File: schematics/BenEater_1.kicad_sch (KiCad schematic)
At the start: 12 parts, among them SW1 RESET, U1 W65C02SxP, U2 28C256, U3 W65C22SxP, U4 74HC00, U6 HM62256BLP, X1 ACO-1 MHz

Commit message: correct schematic
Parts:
- DS1: value WC1602A -> 16x2 LCD
- U6: value HM62256BLP -> 62256
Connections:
- net VCC is gone; now on net +5V: U4.1, U4.2, U4.5
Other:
- note added: "A"
- note added: "K"
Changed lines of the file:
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@@
 		)
 	)
+	(text "A"
+		(exclude_from_sim no)
+		(at 239.522 132.08 0)
+		(effects
+			(font
+				(size 1.27 1.27)
+			)
+		)
+	)
 	(text ""
 		(exclude_from_sim no)
@@
 		)
 	)
+	(text "K"
+		(exclude_from_sim no)
+		(at 239.522 134.874 0)
+		(effects
+			(font
+				(size 1.27 1.27)
+			)
+		)
+	)
 	(label "Reset"
 		(at 26.67 72.39 0)
@@
 		)
 	)
-	(hierarchical_label "VCC"
-		(shape input)
-		(at 40.64 30.48 180)
-		(effects
-			(font
-				(size 1.27 1.27)
-			)
-			(justify right)
-		)
-	)
-	(hierarchical_label "VCC"
-		(shape input)
-		(at 40.64 50.8 180)
-		(effects
-			(font
-				(size 1.27 1.27)
-			)
-			(justify right)
-		)
-	)
-	(hierarchical_label "VCC"
-		(shape input)
-		(at 40.64 35.56 180)
-		(effects
-			(font
-				(size 1.27 1.27)
-			)
-			(justify right)
-		)
-	)
 	(symbol
 		(lib_id "power:GND")
@@
 			)
 		)
-		(property "Value" "WC1602A"
+		(property "Value" "16x2 LCD"
 			(at 242.2241 119.38 0)
 			(effects
@@
 			)
 		)
-		(property "Value" "HM62256BLP"
+		(property "Value" "62256"
 			(at 92.3641 121.92 0)
 			(effects
@@
 	)
 	(symbol
+		(lib_id "power:+5V")
+		(at 40.64 50.8 90)
+		(unit 1)
+		(exclude_from_sim no)
+		(in_bom yes)
+		(on_board yes)
+		(dnp no)
+		(fields_autoplaced yes)
+		(property "Reference" "#PWR021"
+			(at 44.45 50.8 0)
+			(effects
+				(font
+					(size 1.27 1.27)
+				)
+				(hide yes)
+			)
+		)
+		(property "Value" "+5V"
+			(at 36.83 50.7999 90)
+			(effects
+				(font
+					(size 1.27 1.27)
+				)
+				(justify left)
+			)
+		)
+		(property "Footprint" ""
+			(at 40.64 50.8 0)
+			(effects
+				(font
+					(size 1.27 1.27)
+				)
+				(hide yes)
+			)
+		)
+		(property "Datasheet" ""
+			(at 40.64 50.8 0)
+			(effects
+				(font
+					(size 1.27 1.27)
+				)
+				(hide yes)
+			)
+		)
+		(property "Description" "Power symbol creates a global label with name \"+5V\""
+			(at 40.64 50.8 0)
+			(effects
+				(font
+					(size 1.27 1.27)
+				)
+				(hide yes)
+			)
+		)
+		(pin "1"
+		)
+		(instances
+			(project "BenEater_1"
+				(path "/62800d61-69d3-49b6-812a-0798483234f1"
+					(reference "#PWR021")
+					(unit 1)
+				)
+			)
+		)
+	)
+	(symbol
 		(lib_id "74xx:74HC00")
 		(at 48.26 33.02 0)
@@
 					(unit 1)
 				)
+			)
+		)
+	)
+	(symbol
+		(lib_id "power:+5V")
+		(at 40.64 30.48 90)
+		(unit 1)
+		(exclude_from_sim no)
+		(in_bom yes)
+		(on_board yes)
+		(dnp no)
+		(fields_autoplaced yes)
+		(property "Reference" "#PWR019"
+			(at 44.45 30.48 0)
+			(effects
+				(font
+					(size 1.27 1.27)
+				)
+				(hide yes)
+			)
+		)
+		(property "Value" "+5V"
+			(at 36.83 30.4799 90)
+			(effects
+				(font
+					(size 1.27 1.27)
+				)
+				(justify left)
+			)
+		)
+		(property "Footprint" ""
+			(at 40.64 30.48 0)
+			(effects
+				(font
+					(size 1.27 1.27)
+				)
+				(hide yes)
+			)
+		)
+		(property "Datasheet" ""
+			(at 40.64 30.48 0)
+			(effects
+				(font
+					(size 1.27 1.27)
+				)
+				(hide yes)
+			)
+		)
+		(property "Description" "Power symbol creates a global label with name \"+5V\""
+			(at 40.64 30.48 0)
+			(effects
+				(font
+					(size 1.27 1.27)
+				)
+				(hide yes)
+			)
+		)
+		(pin "1"
+		)
+		(instances
+			(project ""
+				(path "/62800d61-69d3-49b6-812a-0798483234f1"
+					(reference "#PWR019")
+					(unit 1)
+				)
+			)
+		)
+	)
+	(symbol
+		(lib_id "power:+5V")
+		(at 40.64 35.56 90)
+		(unit 1)
+		(exclude_from_sim no)
+		(in_bom yes)
+		(on_board yes)
+		(dnp no)
+		(fields_autoplaced yes)
+		(property "Reference" "#PWR020"
+			(at 44.45 35.56 0)
+			(effects
+				(font
+					(size 1.27 1.27)
+				)
+				(hide yes)
+			)
+		)
+		(property "Value" "+5V"
+			(at 36.83 35.5599 90)
+			(effects
+				(font
+					(size 1.27 1.27)
+				)
+				(justify left)
+			)
+		)
+		(property "Footprint" ""
+			(at 40.64 35.56 0)
+			(effects
+				(font
+					(size 1.27 1.27)
+				)
+				(hide yes)
+			)
+		)
+		(property "Datasheet" ""
+			(at 40.64 35.56 0)
+			(effects
+				(font
+					(size 1.27 1.27)
+				)
+				(hide yes)
+			)
+		)
+		(property "Description" "Power symbol creates a global label with name \"+5V\""
+			(at 40.64 35.56 0)
+			(effects
+				(font
+					(size 1.27 1.27)
+				)
+				(hide yes)
+			)
+		)
+		(pin "1"
+		)
+		(instances
+			(project "BenEater_1"
+				(path "/62800d61-69d3-49b6-812a-0798483234f1"
+					(reference "#PWR020")
+					(unit 1)
+				)

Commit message: Update schematic, added DS1813 & SOB connection to the MPU
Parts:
- removed C2: 0.1uF, symbol Device:C
- removed R1: 1k, symbol Device:R
- added DS1813: ~, symbol added_symbols:DS1813-5+T&R
- added R1: 3.3k, symbol Device:R_Small
- SW1: value RESET -> SW_Push
- X1: value ACO-1 MHz -> ACO-1.843 MHz
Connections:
- net +5V: now also DS1813.2 (Vcc), R1.2
- net GND: now also SW1.2, DS1813. (GND); no longer SW1.1
- net RESET: now also SW1.1, DS1813.1 (RSTB); no longer SW1.2
- net at U1.38 (~{SO}): now also R1.1
- no-connect marks 24 -> 23
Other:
- note added: "Shimpy 1.5"
- note removed: "Shimpy 1.0"

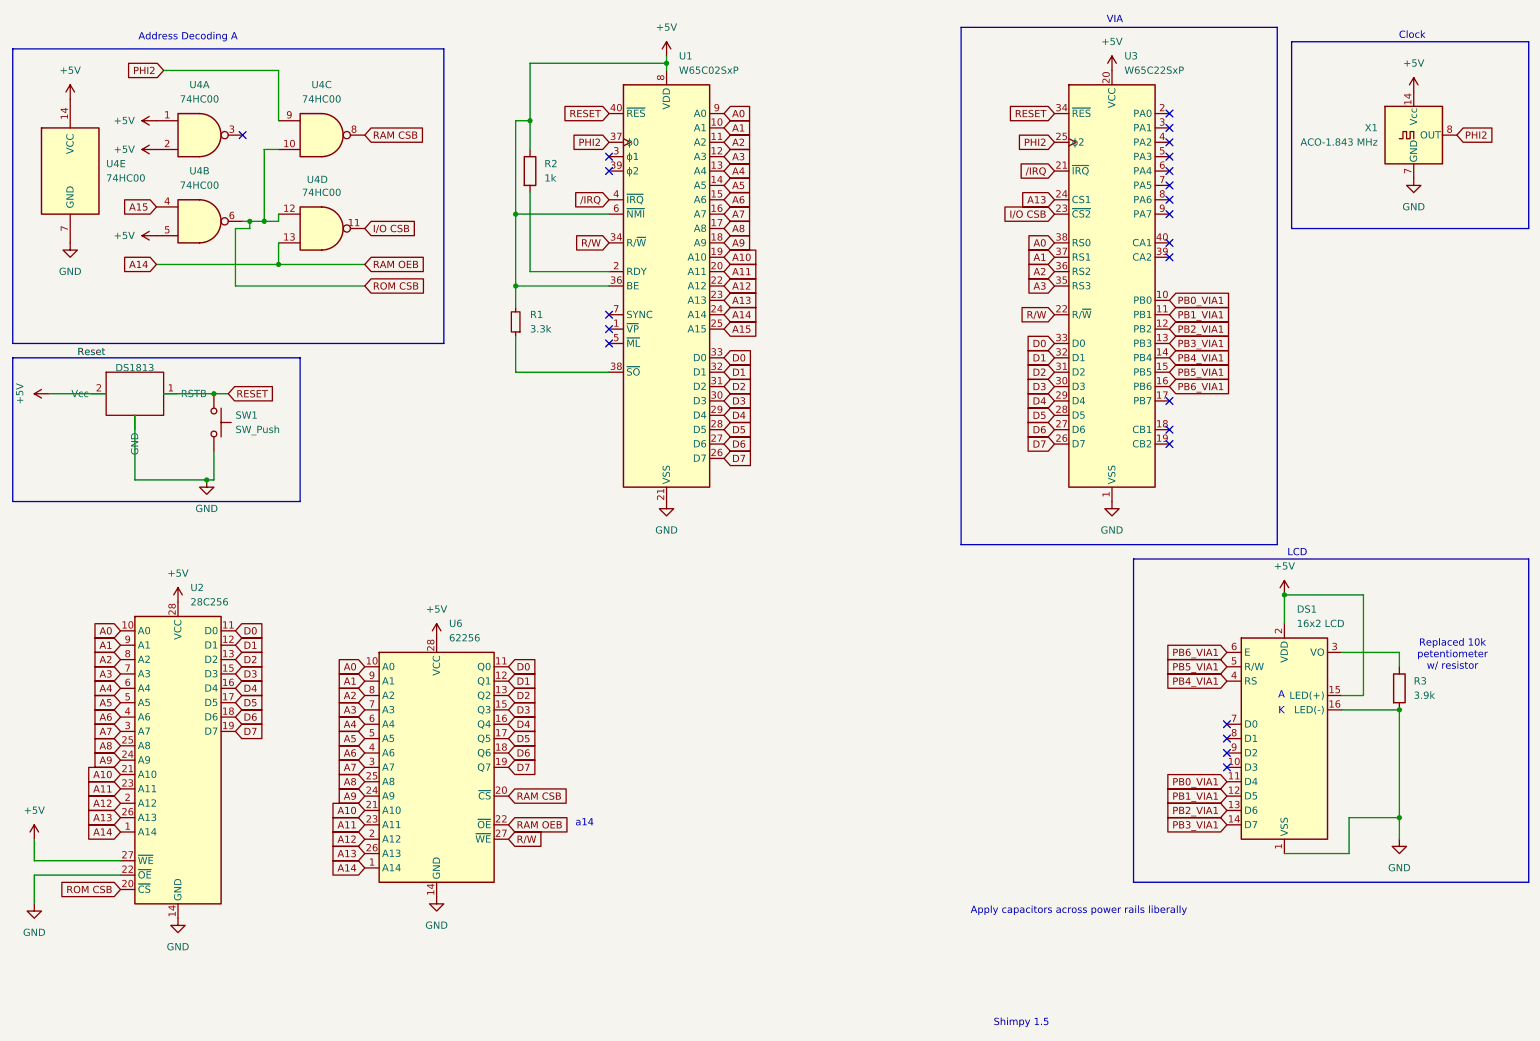
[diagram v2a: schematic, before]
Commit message: Updated schematic to add PLD address decoder & reset supervisor
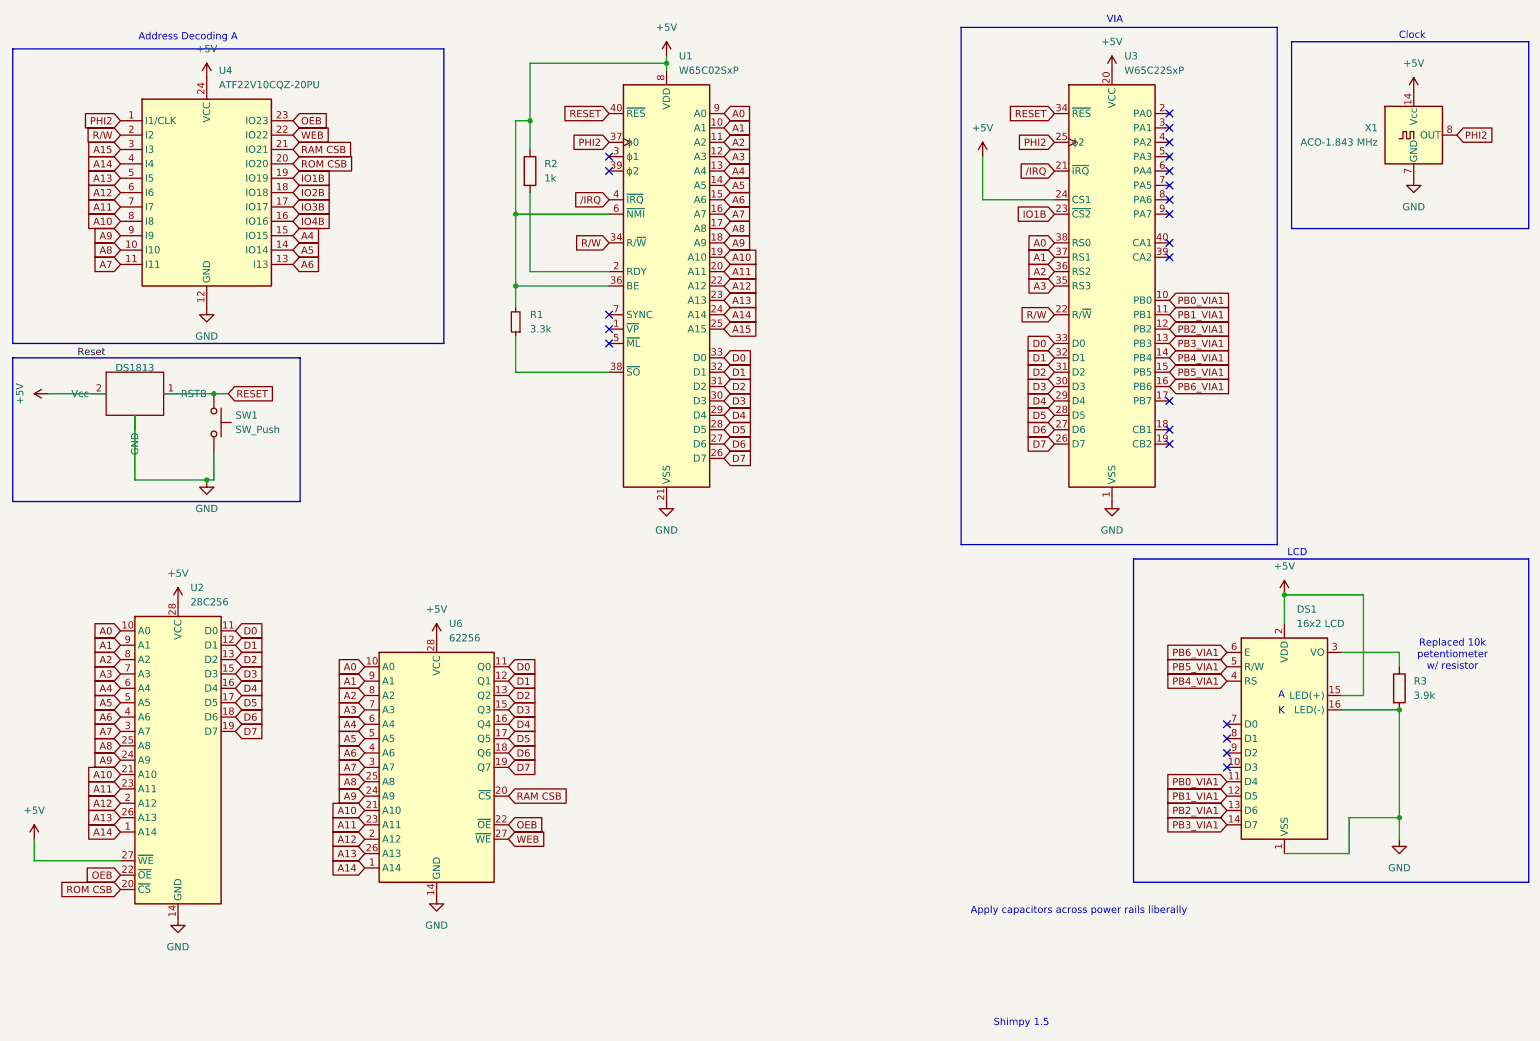
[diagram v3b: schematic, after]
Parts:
- removed U4: 74HC00, symbol 74xx:74HC00
- added U4: ATF22V10CQZ-20PU, Package_DIP:DIP-24_W7.62mm, symbol Logic_Programmable:PEEL22CV10AP
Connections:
- net +5V: now also U3.24 (CS1), U4.24 (VCC)
- net A10: now also U4.8 (I8)
- net A11: now also U4.7 (I7)
- net A12: now also U4.6 (I6)
- net A13: now also U4.5 (I5); no longer U3.24 (CS1)
- net A14: now also U4.4 (I4); no longer U6.22 (~{OE})
- net A15: now also U4.3 (I3)
- net A4: now also U4.15 (IO15)
- net A5: now also U4.14 (IO14)
- net A6: now also U4.13 (I13)
- net A7: now also U4.11 (I11)
- net A8: now also U4.10 (I10)
- net A9: now also U4.9 (I9)
- net GND: now also U4.12 (GND); no longer U2.22 (~{OE})
- net PHI2: now also U4.1 (I1/CLK)
- net RAM CSB: now also U4.21 (IO21)
- net ROM CSB: now also U4.20 (IO20)
- net R/W: now also U4.2 (I2); no longer U6.27 (~{WE})
- net I/O CSB renamed IO1B
- net IO1B: now also U4.19 (IO19)
- new net IO2B: U4.18 (IO18)
- new net IO3B: U4.17 (IO17)
- new net IO4B: U4.16 (IO16)
- new net OEB: U2.22 (~{OE}), U4.23 (IO23), U6.22 (~{OE})
- new net WEB: U4.22 (IO22), U6.27 (~{WE})
- no-connect marks 23 -> 22
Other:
- note removed: "a14"

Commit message: Update schematic
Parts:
- added U5: 74HC11, symbol 74xx:74LS11
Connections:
- net +5V: now also U5.13, U5.14 (VCC), U5.2
- net GND: now also U5.10, U5.11, U5.3, U5.4, U5.5, U5.7 (GND), U5.9
- net /IRQ: now also U5.12; no longer U3.21 (~{IRQ})
- new net VIA1_IRQB: U3.21 (~{IRQ}), U5.1
- no-connect marks 22 -> 24
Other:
- note added: "Interrupt junction"
- note added: "RAM / ROM"
- moved on the sheet: U2, U6
